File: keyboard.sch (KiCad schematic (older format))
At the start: 22 parts, among them IC1 ATMEGA32U4, J1 MINI, P1 CONN_1, P2 CONN_1, P3 CONN_1, P4 CONN_1, P5 CONN_1, P6 CONN_1, X1 ASX3F

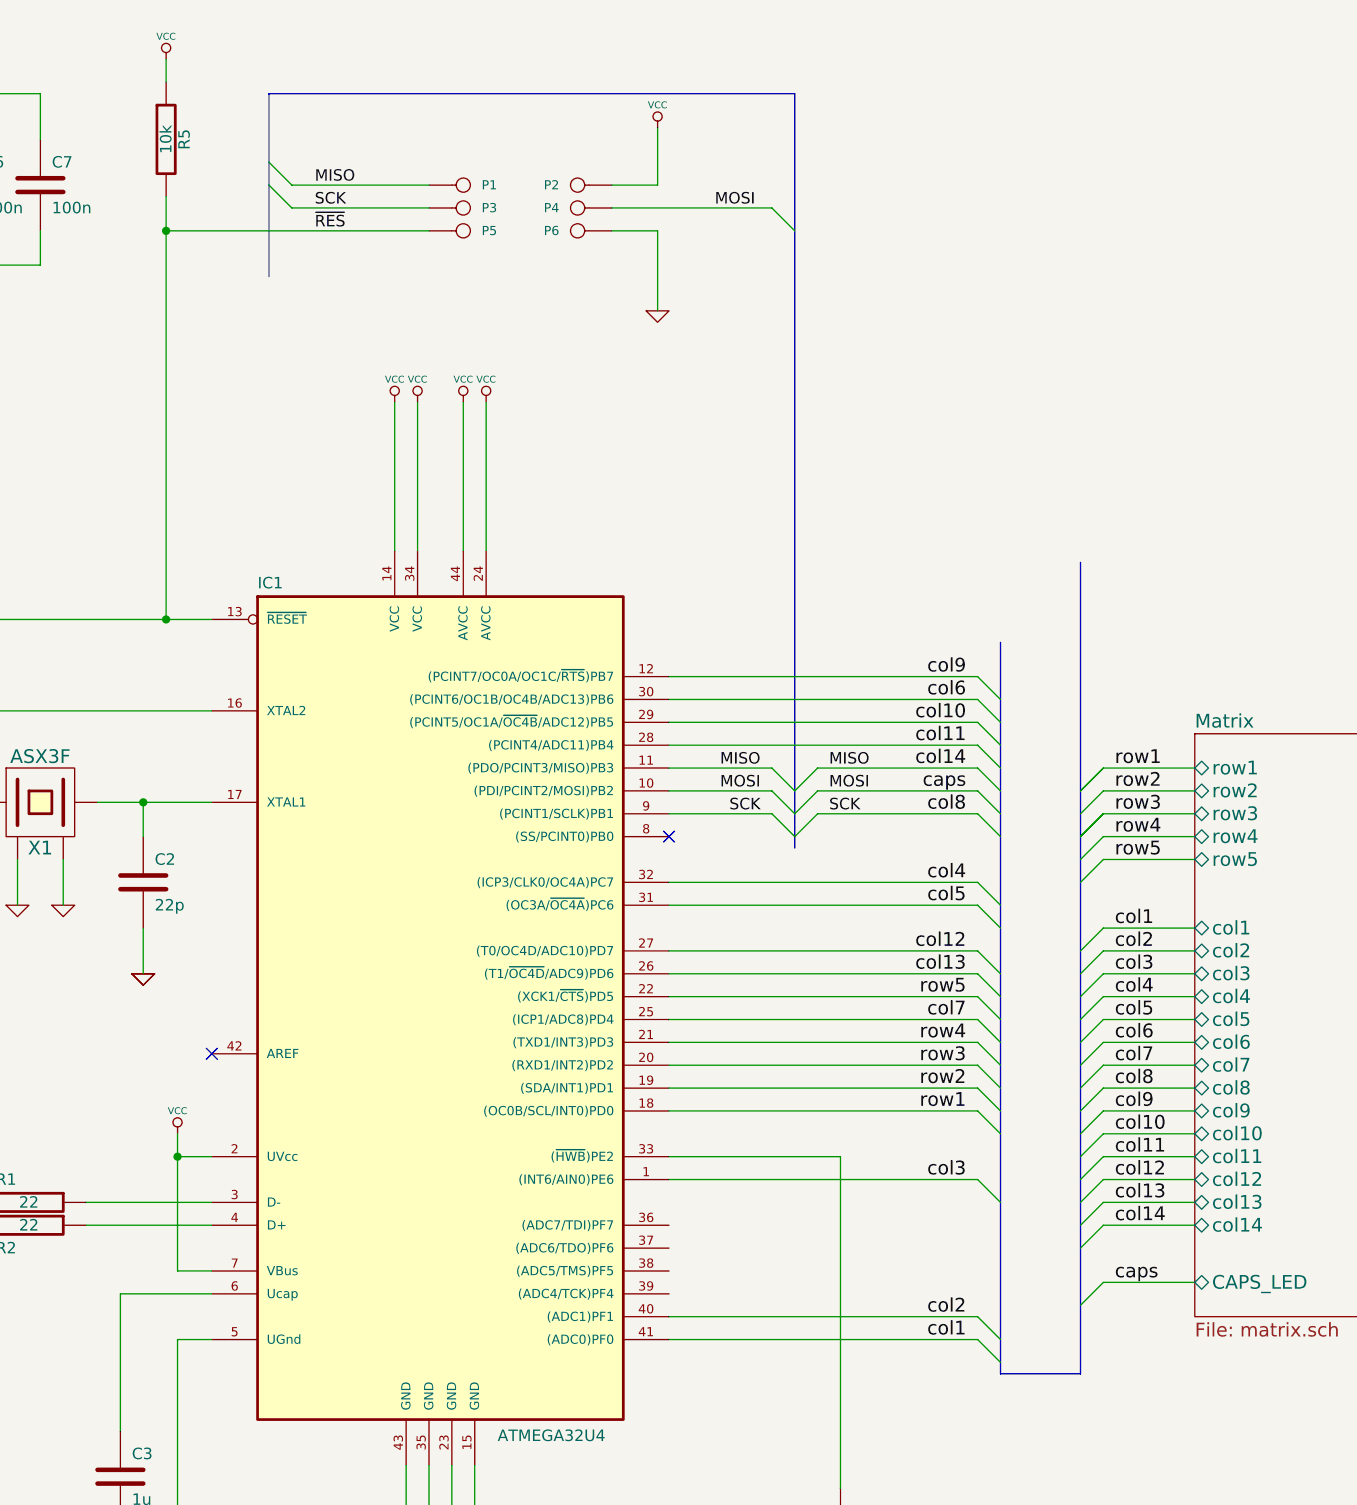
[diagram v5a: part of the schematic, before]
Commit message: Start remapping of rows and cols in MCU
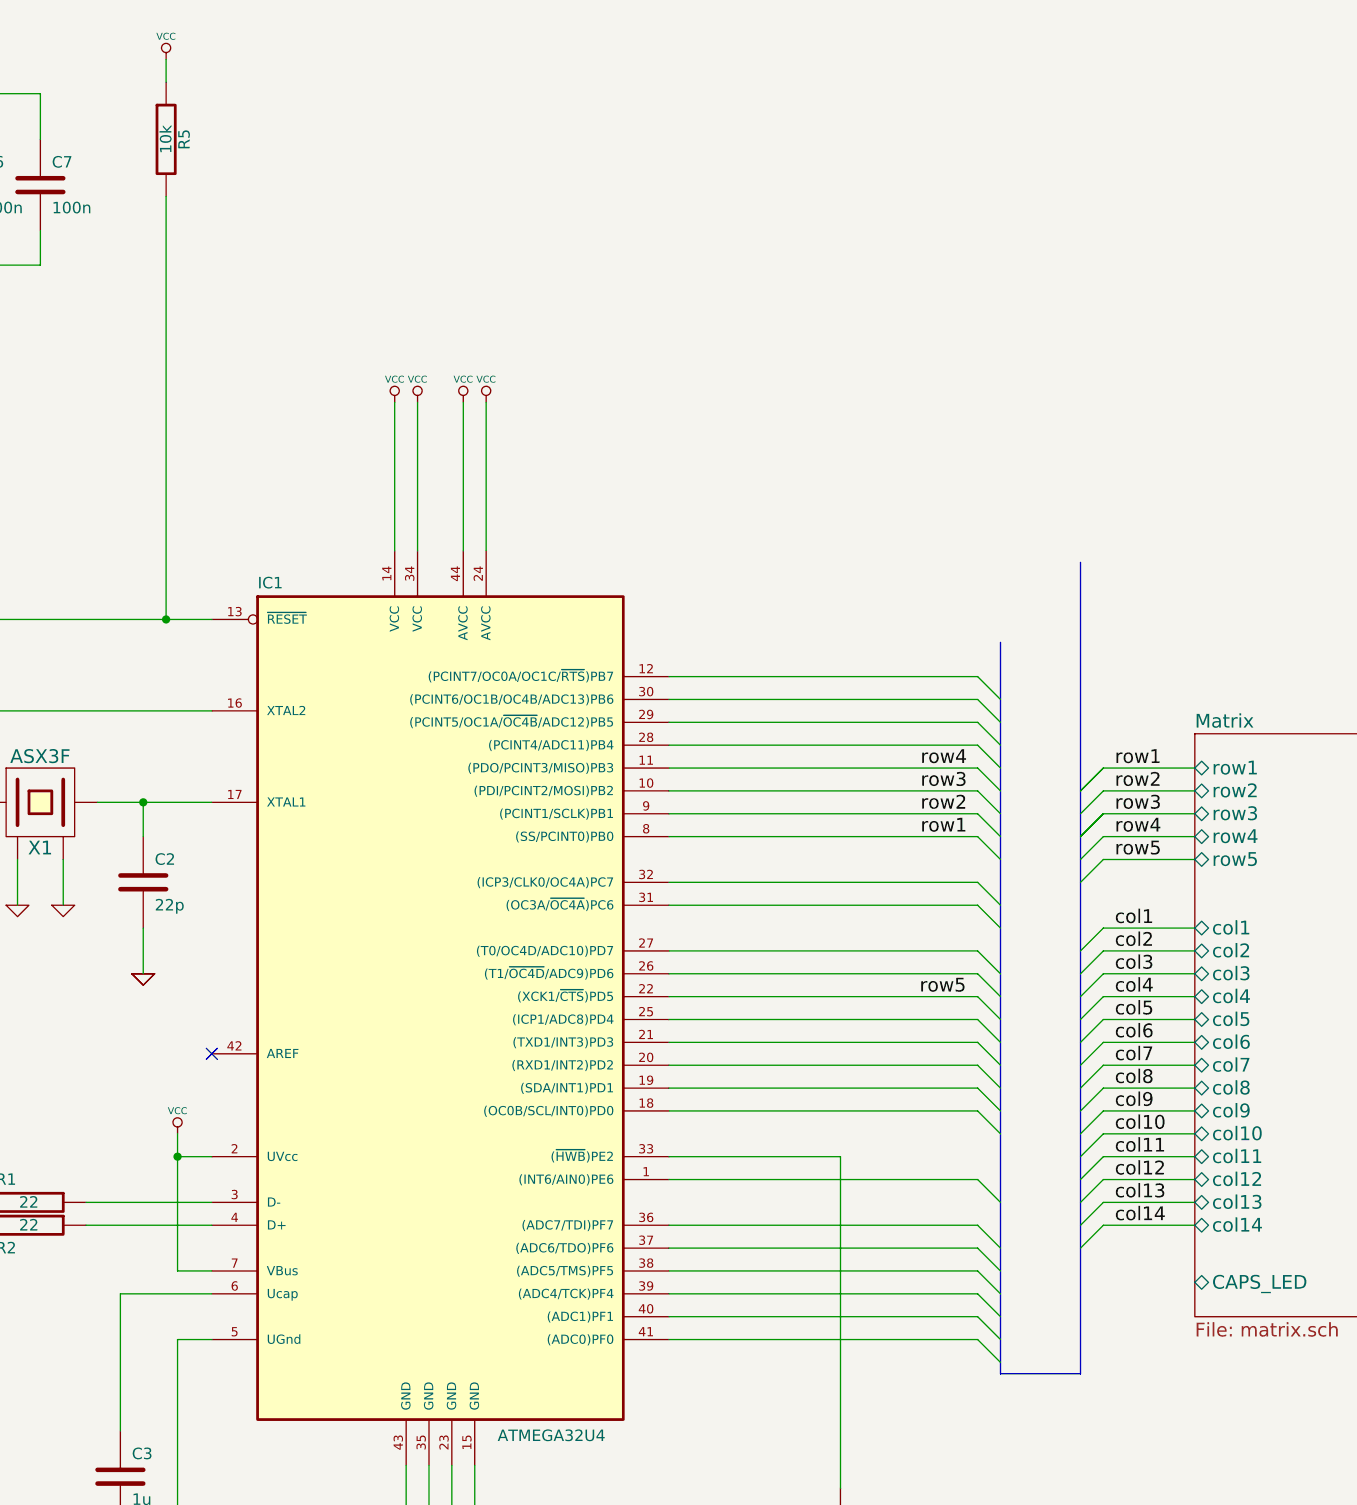
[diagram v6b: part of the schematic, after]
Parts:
- removed P1, P2, P3, P4, P5, P6: CONN_1, symbol conn:CONN_1
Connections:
- net MISO is gone; now on net row4: IC1.11 ((PDO/PCINT3/MISO)PB3)
- net MOSI is gone; now on net row3: IC1.10 ((PDI/PCINT2/MOSI)PB2)
- net SCK is gone; now on net row2: IC1.9 ((PCINT1/SCLK)PB1)
- net col1: no longer IC1.41 ((ADC0)PF0)
- net col10: no longer IC1.29 ((PCINT5/OC1A/~OC4B~/ADC12)PB5)
- net col11: no longer IC1.28 ((PCINT4/ADC11)PB4)
- net col12: no longer IC1.27 ((T0/OC4D/ADC10)PD7)
- net col13: no longer IC1.26 ((T1/~OC4D~/ADC9)PD6)
- net col2: no longer IC1.40 ((ADC1)PF1)
- net col3: no longer IC1.1 ((INT6/AIN0)PE6)
- net col4: no longer IC1.32 ((ICP3/CLK0/OC4A)PC7)
- net col5: no longer IC1.31 ((OC3A/~OC4A~)PC6)
- net col6: no longer IC1.30 ((PCINT6/OC1B/OC4B/ADC13)PB6)
- net col7: no longer IC1.25 ((ICP1/ADC8)PD4)
- net col9: no longer IC1.12 ((PCINT7/OC0A/OC1C/~RTS~)PB7)
- net row1: now also IC1.8 ((SS/PCINT0)PB0); no longer IC1.18 ((OC0B/SCL/INT0)PD0)
- net row2: no longer IC1.19 ((SDA/INT1)PD1)
- net row3: no longer IC1.20 ((RXD1/INT2)PD2)
- net row4: no longer IC1.21 ((TXD1/INT3)PD3)
- net ~RES~: no longer names the net of IC1.13 (~RESET~), R5.2, S0.3
- no-connect marks 5 -> 4
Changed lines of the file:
@@
 Comment4 ""
 $EndDescr
-Text Label 5450 4050 0    50   ~ 0
-SCK
-Text Label 5450 3950 0    50   ~ 0
-MOSI
-Text Label 5450 3850 0    50   ~ 0
-MISO
-Entry Wire Line
-	5300 4150 5400 4050
-Entry Wire Line
-	5300 4050 5400 3950
-Entry Wire Line
-	5300 3950 5400 3850
-Entry Wire Line
-	5200 1400 5300 1500
 $Comp
 L power1:VCC #PWR01
@@
 	1    0    0    -1
 $EndComp
-$Comp
-L power1:VCC #PWR05
-U 1 1 4ED6BD35
-P 4700 1050
-F 0 "#PWR05" H 4700 1150 30  0001 C CNN
-F 1 "VCC" H 4700 1150 30  0000 C CNN
-F 2 "" H 4700 1050 60  0001 C CNN
-F 3 "" H 4700 1050 60  0001 C CNN
-	1    4700 1050
-	1    0    0    -1
-$EndComp
-$Comp
-L power1:GND #PWR06
-U 1 1 4ED6BD03
-P 4700 1850
-F 0 "#PWR06" H 4700 1850 30  0001 C CNN
-F 1 "GND" H 4700 1780 30  0001 C CNN
-F 2 "" H 4700 1850 60  0001 C CNN
-F 3 "" H 4700 1850 60  0001 C CNN
-	1    4700 1850
-	1    0    0    -1
-$EndComp
-Text Label 3200 1500 0    50   ~ 0
-~RES~
-Text Label 4950 1400 0    50   ~ 0
-MOSI
-Text Label 3200 1400 0    50   ~ 0
-SCK
-Text Label 3200 1300 0    50   ~ 0
-MISO
-Entry Wire Line
-	3000 1300 3100 1400
-Entry Wire Line
-	3000 1200 3100 1300
 $Comp
 L power1:GND #PWR07
@@
 	1    0    0    -1
 $EndComp
-Text Label 5150 4050 2    50   ~ 0
-SCK
-Text Label 5150 3950 2    50   ~ 0
-MOSI
-Text Label 5150 3850 2    50   ~ 0
-MISO
-Entry Wire Line
-	5200 3850 5300 3950
-Entry Wire Line
-	5200 3950 5300 4050
-Entry Wire Line
-	5200 4050 5300 4150
 $Comp
 L power1:GND #PWR017
@@
 	6100 3850 6200 3950
 Entry Wire Line
-	6100 3950 6200 4050
-Entry Wire Line
 	6100 4050 6200 4150
 Entry Wire Line
@@
 	0    1    1    0
 $EndComp
-Text Label 6050 5350 2    60   ~ 0
-row1
-Text Label 6050 5250 2    60   ~ 0
-row2
-Text Label 6050 5150 2    60   ~ 0
-row3
-Text Label 6050 5050 2    60   ~ 0
-row4
-Text Label 6050 4850 2    60   ~ 0
-row5
 Entry Wire Line
 	6550 3950 6650 3850
@@
 Text Label 6700 4250 0    60   ~ 0
 row5
-Text Label 6050 6250 2    60   ~ 0
-col2
-Text Label 6050 6350 2    60   ~ 0
-col1
-Text Label 6050 5650 2    60   ~ 0
-col3
 Entry Wire Line
 	6100 4350 6200 4450
-Text Label 6050 4350 2    60   ~ 0
-col4
-Text Label 6050 4450 2    60   ~ 0
-col5
-Text Label 6050 3550 2    60   ~ 0
-col6
 Entry Wire Line
 	6550 4650 6650 4550
@@
 Text Label 6700 5050 0    60   ~ 0
 col6
-Text Label 6050 3650 2    60   ~ 0
-col10
-Text Label 6050 3750 2    60   ~ 0
-col11
-Text Label 6050 4650 2    60   ~ 0
-col12
 Text Label 6700 5150 0    60   ~ 0
 col7
@@
 Entry Wire Line
 	6550 5450 6650 5350
-Text Label 6050 3450 2    60   ~ 0
-col9
 Text Label 6700 5450 0    60   ~ 0
 col10
 Entry Wire Line
 	6550 5550 6650 5450
-Text Label 6050 4750 2    60   ~ 0
-col13
-Text Label 6050 4950 2    60   ~ 0
-col7
 Text Label 6700 5750 0    60   ~ 0
 col13
@@
 Text Label 6700 5550 0    60   ~ 0
 col11
-Text Label 6050 4050 2    60   ~ 0
-col8
 Text Label 6700 5650 0    60   ~ 0
 col12
 Entry Wire Line
 	6550 5750 6650 5650
-Text Label 6050 3950 2    60   ~ 0
-caps
-Text Label 6700 6100 0    60   ~ 0
-caps
-Entry Wire Line
-	6550 6200 6650 6100
-Text Label 6050 3850 2    60   ~ 0
-col14
-$Comp
-L conn:CONN_1 P1
-U 1 1 507D1E9B
-P 3850 1300
-F 0 "P1" H 3930 1300 40  0000 L CNN
-F 1 "CONN_1" H 3850 1355 30  0001 C CNN
-F 2 "" H 3850 1300 60  0001 C CNN
-F 3 "" H 3850 1300 60  0001 C CNN
-	1    3850 1300
-	1    0    0    -1
-$EndComp
-$Comp
-L conn:CONN_1 P3
-U 1 1 507D1EE6
-P 3850 1400
-F 0 "P3" H 3930 1400 40  0000 L CNN
-F 1 "CONN_1" H 3850 1455 30  0001 C CNN
-F 2 "" H 3850 1400 60  0001 C CNN
-F 3 "" H 3850 1400 60  0001 C CNN
-	1    3850 1400
-	1    0    0    -1
-$EndComp
-$Comp
-L conn:CONN_1 P5
-U 1 1 507D1F31
-P 3850 1500
-F 0 "P5" H 3930 1500 40  0000 L CNN
-F 1 "CONN_1" H 3850 1555 30  0001 C CNN
-F 2 "" H 3850 1500 60  0001 C CNN
-F 3 "" H 3850 1500 60  0001 C CNN
-	1    3850 1500
-	1    0    0    -1
-$EndComp
-$Comp
-L conn:CONN_1 P2
-U 1 1 507D1F7C
-P 4350 1300
-F 0 "P2" H 4430 1300 40  0000 L CNN
-F 1 "CONN_1" H 4350 1355 30  0001 C CNN
-F 2 "" H 4350 1300 60  0001 C CNN
-F 3 "" H 4350 1300 60  0001 C CNN
-	1    4350 1300
-	-1   0    0    1
-$EndComp
-$Comp
-L conn:CONN_1 P4
-U 1 1 507D1FC7
-P 4350 1400
-F 0 "P4" H 4430 1400 40  0000 L CNN
-F 1 "CONN_1" H 4350 1455 30  0001 C CNN
-F 2 "" H 4350 1400 60  0001 C CNN
-F 3 "" H 4350 1400 60  0001 C CNN
-	1    4350 1400
-	-1   0    0    1
-$EndComp
-$Comp
-L conn:CONN_1 P6
-U 1 1 507D2012
-P 4350 1500
-F 0 "P6" H 4430 1500 40  0000 L CNN
-F 1 "CONN_1" H 4350 1555 30  0001 C CNN
-F 2 "" H 4350 1500 60  0001 C CNN
-F 3 "" H 4350 1500 60  0001 C CNN
-	1    4350 1500
-	-1   0    0    1
-$EndComp
 $Comp
 L device:C C8
@@
 	800  3200 1050 3200
 Wire Wire Line
-	5200 1400 4500 1400
-Wire Wire Line
-	3100 1300 3700 1300
-Wire Wire Line
 	4750 5650 6100 5650
 Wire Wire Line
-	6100 3950 5400 3950
-Wire Wire Line
 	6100 3750 4750 3750
 Wire Wire Line
@@
 	5500 5550 5500 7000
 Wire Wire Line
-	4700 1300 4700 1050
-Wire Wire Line
-	4500 1300 4700 1300
-Wire Wire Line
 	2550 750  2550 850
-Wire Wire Line
-	4750 3950 5200 3950
 Wire Wire Line
 	5500 7650 5500 7500
@@
 	2600 5450 2600 5550
 Connection ~ 2600 5550
-Wire Wire Line
-	4750 3850 5200 3850
-Wire Wire Line
-	4750 4050 5200 4050
-Wire Wire Line
-	2550 1350 2550 1500
 Connection ~ 2550 3200
 Wire Wire Line
-	4700 1500 4500 1500
-Wire Wire Line
-	4700 1850 4700 1500
-Wire Wire Line
 	1750 4000 1550 4000
 Wire Wire Line
@@
 	4750 3650 6100 3650
 Wire Wire Line
-	5400 3850 6100 3850
-Wire Wire Line
-	6100 4050 5400 4050
-Wire Wire Line
 	4750 4450 6100 4450
 Wire Wire Line
-	3100 1400 3700 1400
-Wire Wire Line
 	1450 3200 2550 3200
 Wire Wire Line
@@
 	7050 5650 6650 5650
 Wire Wire Line
-	6650 6100 7050 6100
-Wire Wire Line
 	4750 6250 6100 6250
 Wire Wire Line
 	4750 6350 6100 6350
-Wire Bus Line
-	3000 900  5300 900
-Wire Wire Line
-	3700 1500 2550 1500
-Connection ~ 2550 1500
 Wire Bus Line
 	6550 6500 6200 6500
@@
 NoConn ~ 1050 3300
 NoConn ~ 2750 5100
-NoConn ~ 4750 4150
 Wire Wire Line
 	1100 900  1100 1100
@@
 	2550 3200 2750 3200
 Wire Wire Line
-	2550 1500 2550 3200
-Wire Wire Line
 	800  900  800  1100
 Wire Wire Line
 	800  1650 800  1900
+Wire Wire Line
+	4750 3850 6100 3850
+Wire Wire Line
+	4750 4050 6100 4050
+Entry Wire Line
+	6100 3950 6200 4050
+Wire Wire Line
+	4750 3950 6100 3950
+Entry Wire Line
+	6100 4150 6200 4250
+Wire Wire Line
+	4750 4150 6100 4150
+Text Label 5850 4150 0    60   ~ 0
+row1
+Text Label 6050 4850 2    60   ~ 0
+row5
+Entry Wire Line
+	6100 6150 6200 6250
+Entry Wire Line
+	6100 6050 6200 6150
+Entry Wire Line
+	6100 5950 6200 6050
+Entry Wire Line
+	6100 5850 6200 5950
+Wire Wire Line
+	4750 5850 6100 5850
+Wire Wire Line
+	4750 5950 6100 5950
+Wire Wire Line
+	4750 6050 6100 6050
+Wire Wire Line
+	4750 6150 6100 6150
+Text Label 5850 4050 0    60   ~ 0
+row2
+Text Label 5850 3950 0    60   ~ 0
+row3
+Text Label 5850 3850 0    60   ~ 0
+row4
+Wire Wire Line
+	2550 1350 2550 3200
 Wire Bus Line
-	3000 900  3000 1700
-Wire Bus Line
-	5300 900  5300 4200
+	6550 2950 6550 6500
 Wire Bus Line
 	6200 3300 6200 6500
-Wire Bus Line
-	6550 2950 6550 6500
 $EndSCHEMATC

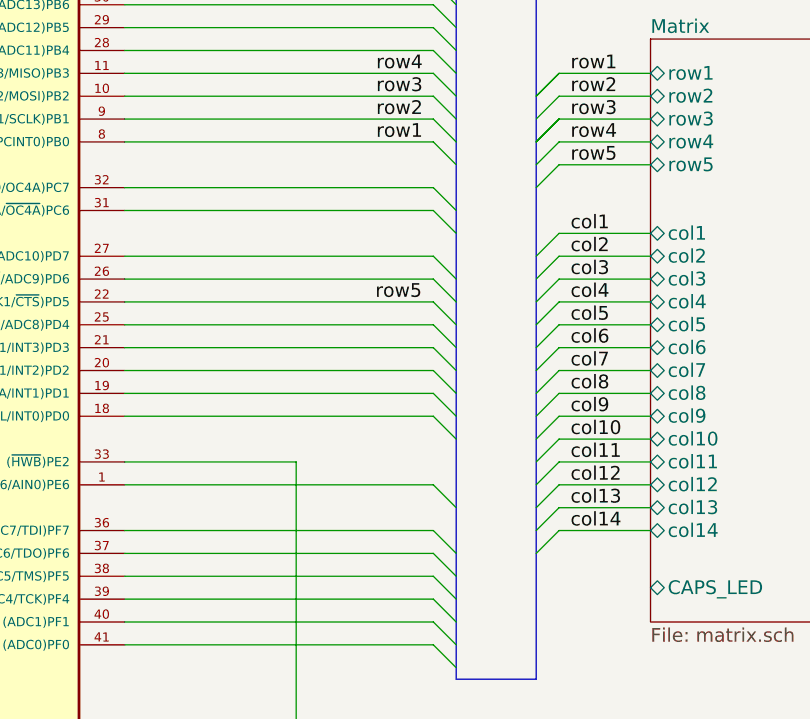
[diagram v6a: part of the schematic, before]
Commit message: Connect cols 1 to 3
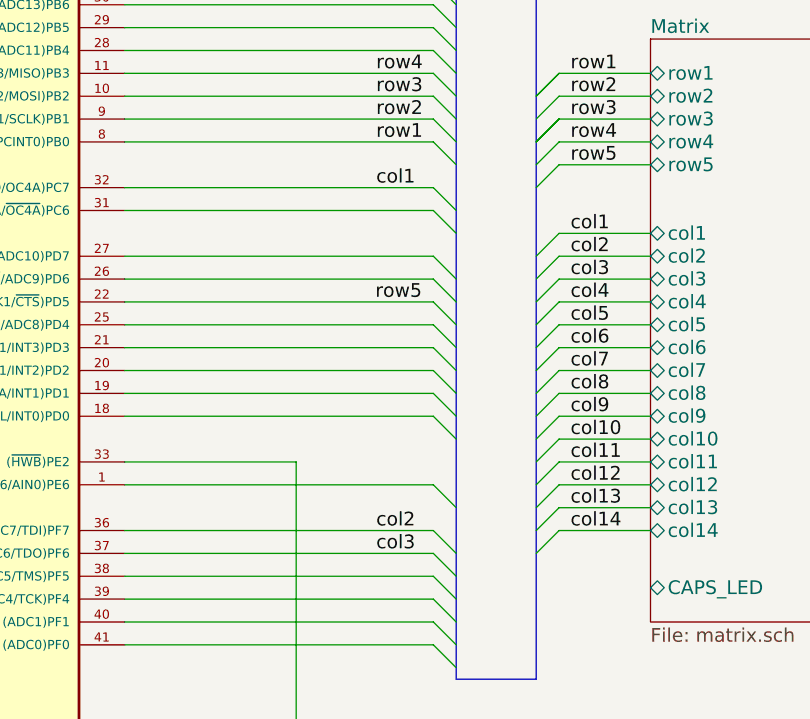
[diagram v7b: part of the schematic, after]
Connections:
- net col1: now also IC1.32 ((ICP3/CLK0/OC4A)PC7)
- net col2: now also IC1.36 ((ADC7/TDI)PF7)
- net col3: now also IC1.37 ((ADC6/TDO)PF6)
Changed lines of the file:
@@
 Wire Bus Line
 	6200 3300 6200 6500
+Text Label 5850 4350 0    60   ~ 0
+col1
+Text Label 5850 5850 0    60   ~ 0
+col2
+Text Label 5850 5950 0    60   ~ 0
+col3
 $EndSCHEMATC

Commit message: Connect col4
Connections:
- net col4: now also IC1.38 ((ADC5/TMS)PF5)
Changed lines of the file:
@@
 Text Label 5850 5950 0    60   ~ 0
 col3
+Text Label 5850 6050 0    60   ~ 0
+col4
 $EndSCHEMATC
